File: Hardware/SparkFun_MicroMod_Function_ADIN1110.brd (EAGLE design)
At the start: 38 x 65 mm, 115 parts, among them J1 IP20(RJ50), J2 MICROMOD_FUNCTION_STANDARD, Q1 220mA/50V/3.5Ω, Q2 20V/4.2A/52mΩ/1.4W, T1 WE-STST, U1 ADIN1110, U2 EEPROM, U3 3.3V, U4 WE-TVS, Y1 25MHz

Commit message: R3, R4, R5, R6 to in-house PROD_IDs
Note, these values are very slightly different than the ones in the DS sch.
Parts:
- R3, R4: value 5.1Ω -> 4.7
- R5, R6: value 10.2Ω -> 10Ω
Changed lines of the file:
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@@
 <attribute name="VALUE" value="Blue" x="28.575040625" y="63.0764" size="0.6096" layer="27" font="vector" ratio="20" rot="R90" align="top-center"/>
 </element>
-<element name="R5" library="SparkFun-Resistors" package="0402-TIGHT" value="10.2Ω" x="20.812759375" y="39.8145" smashed="yes">
+<element name="R5" library="SparkFun-Resistors" package="0402-TIGHT" value="10Ω" x="20.812759375" y="39.8145" smashed="yes">
 <attribute name="NAME" x="20.812759375" y="40.3765" size="0.6096" layer="25" font="vector" ratio="20" align="bottom-center"/>
-<attribute name="VALUE" x="22.89301875" y="40.1542" size="0.6096" layer="27" font="vector" ratio="20" align="top-center"/>
+<attribute name="PROD_ID" value="RES-16072" x="20.812759375" y="39.8145" size="1.778" layer="27" display="off"/>
+<attribute name="VALUE" value="10Ω" x="22.89301875" y="40.1542" size="0.6096" layer="27" font="vector" ratio="20" align="top-center"/>
 </element>
-<element name="R6" library="SparkFun-Resistors" package="0402-TIGHT" value="10.2Ω" x="20.289521875" y="38.89501875" smashed="yes">
+<element name="R6" library="SparkFun-Resistors" package="0402-TIGHT" value="10Ω" x="20.289521875" y="38.89501875" smashed="yes">
 <attribute name="NAME" x="20.289521875" y="39.45701875" size="0.6096" layer="25" font="vector" ratio="20" align="bottom-center"/>
-<attribute name="VALUE" x="22.308821875" y="39.1661375" size="0.6096" layer="27" font="vector" ratio="20" align="top-center"/>
+<attribute name="PROD_ID" value="RES-16072" x="20.289521875" y="38.89501875" size="1.778" layer="27" display="off"/>
+<attribute name="VALUE" value="10Ω" x="22.308821875" y="39.1661375" size="0.6096" layer="27" font="vector" ratio="20" align="top-center"/>
 </element>
-<element name="R4" library="SparkFun-Resistors" package="0402-TIGHT" value="5.1Ω" x="22.501859375" y="42.4459375" smashed="yes" rot="R180">
+<element name="R4" library="SparkFun-Resistors" package="0402-TIGHT" value="4.7" x="22.501859375" y="42.4459375" smashed="yes" rot="R180">
 <attribute name="NAME" x="22.501859375" y="41.8839375" size="0.6096" layer="25" font="vector" ratio="20" rot="R180" align="bottom-center"/>
-<attribute name="VALUE" x="24.462740625" y="42.1697375" size="0.6096" layer="27" font="vector" ratio="20" rot="R180" align="top-center"/>
+<attribute name="PROD_ID" value="RES-16312" x="22.501859375" y="42.4459375" size="1.778" layer="27" rot="R180" display="off"/>
+<attribute name="VALUE" value="4.7" x="24.462740625" y="42.1697375" size="0.6096" layer="27" font="vector" ratio="20" rot="R180" align="top-center"/>
 </element>
-<element name="R3" library="SparkFun-Resistors" package="0402-TIGHT" value="5.1Ω" x="18.54961875" y="42.420540625" smashed="yes" rot="R180">
+<element name="R3" library="SparkFun-Resistors" package="0402-TIGHT" value="4.7" x="18.54961875" y="42.420540625" smashed="yes" rot="R180">
 <attribute name="NAME" x="18.54961875" y="41.858540625" size="0.6096" layer="25" font="vector" ratio="20" rot="R180" align="bottom-center"/>
-<attribute name="VALUE" x="16.624296875" y="42.1672" size="0.6096" layer="27" font="vector" ratio="20" rot="R180" align="top-center"/>
+<attribute name="PROD_ID" value="RES-16312" x="18.54961875" y="42.420540625" size="1.778" layer="27" rot="R180" display="off"/>
+<attribute name="VALUE" value="4.7" x="16.624296875" y="42.1672" size="0.6096" layer="27" font="vector" ratio="20" rot="R180" align="top-center"/>
 </element>
 <element name="C2" library="SparkFun-Capacitors" package="0603" value="0.22uF" x="18.7934625" y="43.6981625" smashed="yes">

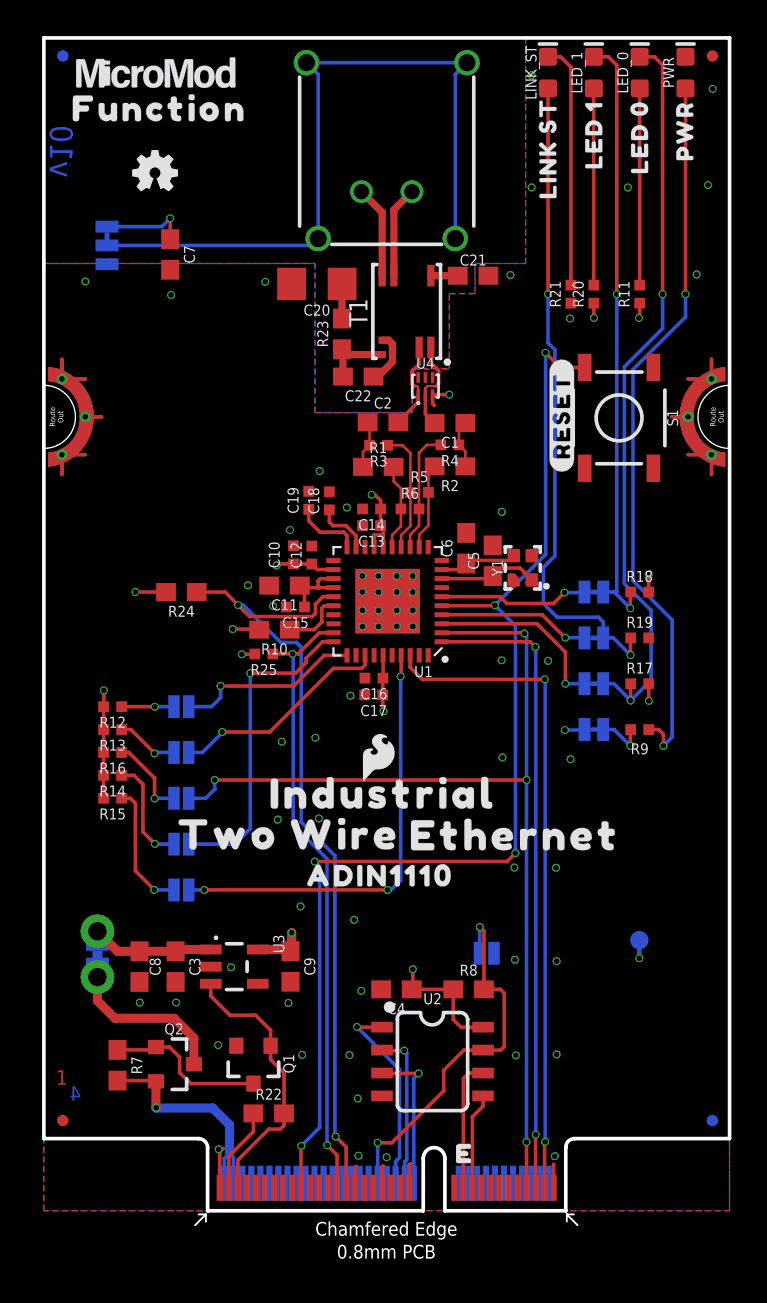
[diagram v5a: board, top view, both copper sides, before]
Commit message: TVS diode placement and more
-Moved TVS diodes to "IC" side of DA-/DA+ DC coupling caps
-Added debounce to reset button
-Routed through pads 5 and 6 on TVS diode package.
-Added R29 to avoid damaging GPIO if set to output low and button pressed
-Added R26 to mosfet gate control line to avoid potential overvoltage/ringing
-Re-arranged caps so smalled value decoupling caps are closest to pins on IC.
-moved to "v10" in brd and sch
-C22 changed to 470nF to improove droop performance
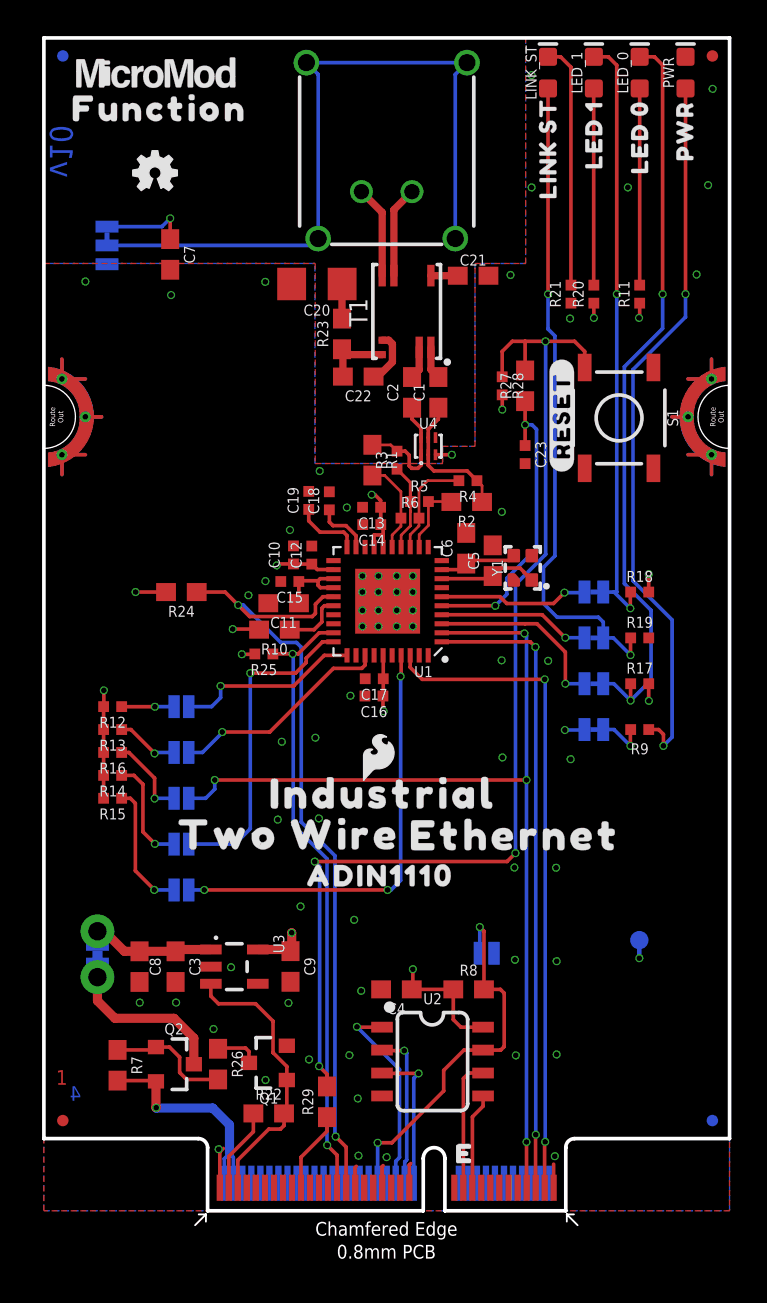
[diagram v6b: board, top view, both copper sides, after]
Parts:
- added C23: 0.1uF, SparkFun-Capacitors:0402-TIGHT
- added R26: 100, SparkFun-Resistors:0603
- added R27: 10k, SparkFun-Resistors:0603
- added R28: 100k, SparkFun-Resistors:0402-TIGHT
- added R29: 100Ω, SparkFun-Resistors:0603
- C22: value 0.1uF -> 470nF
- R3, R4: value 4.7 -> 5.1k
- R5, R6: value 10Ω -> 10.2k
- moved U4 3.33 mm to (21.3, 42.4)
- moved C2 2.31 mm to (20.4, 45.4), turned to 90 degrees
- moved R4 2.22 mm to (23.5, 40.5)
- moved R2 2.18 mm to (23.4, 39.3)
- moved C1 1.82 mm to (21.9, 45.4), turned to 90 degrees
- moved C15 1.44 mm to (13.6, 34.9)
- moved R3 1.31 mm to (19.6, 41.6), turned to 90 degrees
- moved C13 1.01 mm to (18.2, 39.0)
- moved C16 0.99 mm to (18.3, 28.5)
- moved C11 0.98 mm to (13.3, 33.7)
- moved C17 0.90 mm to (18.3, 29.5)
- moved C14 0.87 mm to (18.2, 38.0)
- moved Q1 0.85 mm to (12.5, 8.20), turned to 90 degrees
- moved R5 0.51 mm to (20.8, 39.3)
- moved R6 0.51 mm to (20.3, 38.4)
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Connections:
- new net N$10: Q1.3, R26.1
- new net N$13: C23.1, R27.1, U1.5
- new net N$15: R27.2, R28.1, R29.2, S1.3
- net !RESET!: now also R29.1; no longer S1.3, U1.5
- net 3.3V: now also R28.2
- net GND: now also C23.2
- net N$11: now also R26.2; no longer Q1.3
- net N$24: now also U4.2, U4.5
- net N$31: now also U4.1, U4.6
- net N$32: no longer U4.2
- net N$34: no longer U4.1
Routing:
- net N$15: track 0.00 -> 62.1 mm, vias 0 -> 4
- net !RESET!: track 64.8 -> 4.51 mm, vias 5 -> 0
- net N$13: track 0.00 -> 16.9 mm, vias 0 -> 2
- net N$24: track 2.69 -> 7.77 mm
- net N$31: track 2.67 -> 7.05 mm
- net N$32: track 5.18 -> 1.81 mm
- net N$34: track 4.99 -> 1.80 mm
- net N$10: track 0.00 -> 2.44 mm
- net N$11: track 8.93 -> 6.87 mm
- net N$36: track 6.86 -> 4.83 mm
- net N$35: track 6.82 -> 5.82 mm
- net 3.3V: track 36.4 -> 37.3 mm, vias 15 -> 16
- net N$38: track 4.83 -> 4.02 mm
- net GND: track 9.56 -> 9.04 mm, vias 64 -> 65
- net PWR_EN: track 15.3 -> 15.8 mm

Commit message: 470pF cap to 0805 with new PROD_ID
-new 470nF cap had to bump up to 0805 for the 100V rating in that value
-Voltage specs in part values
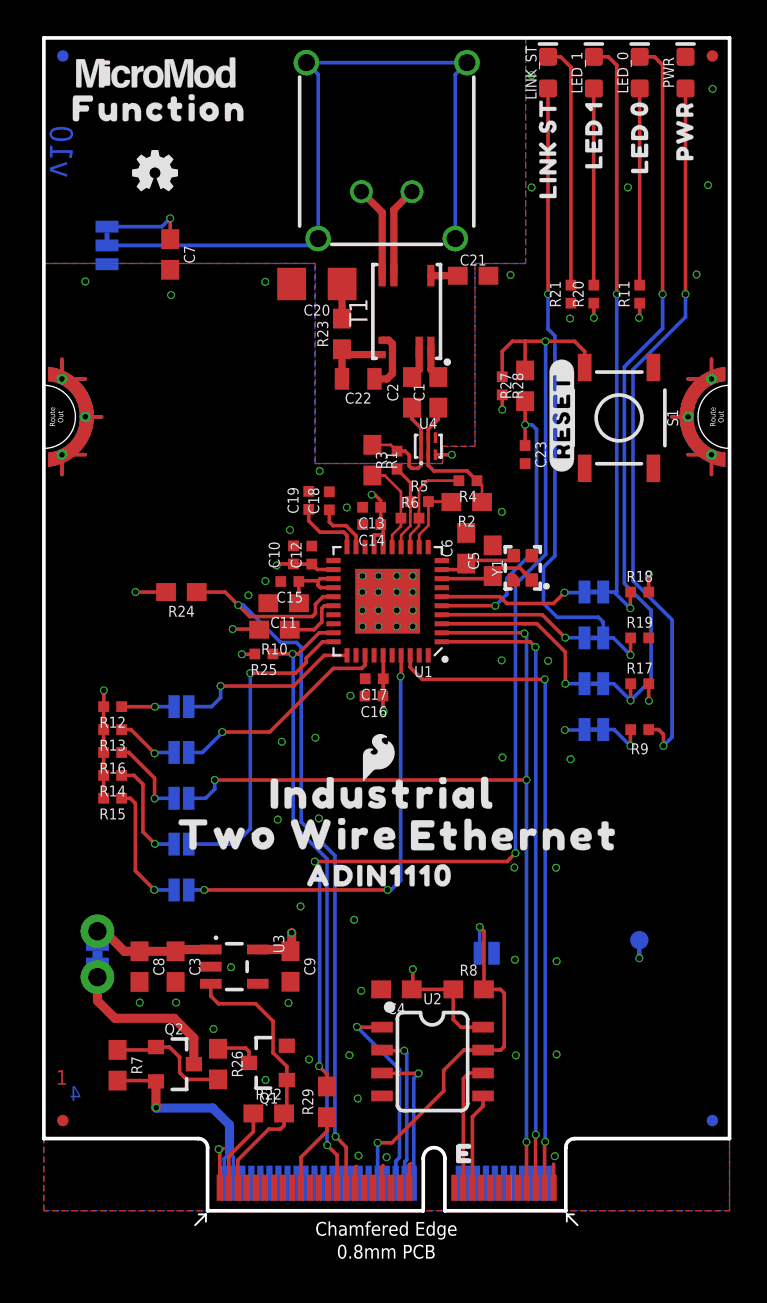
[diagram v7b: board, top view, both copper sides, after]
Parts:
- C21: value 0.1uF -> 0.1uF/50V
- C22: value 470nF -> 470nF/100V; device SparkFun-Capacitors:0603 -> SparkFun-Capacitors:0805
- moved C22 0.13 mm to (17.4, 46.1)

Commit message: SPI test points and moved config jumpers
-moved bottom config jumpers to avoid reflections on CIPO
-added SPI test points
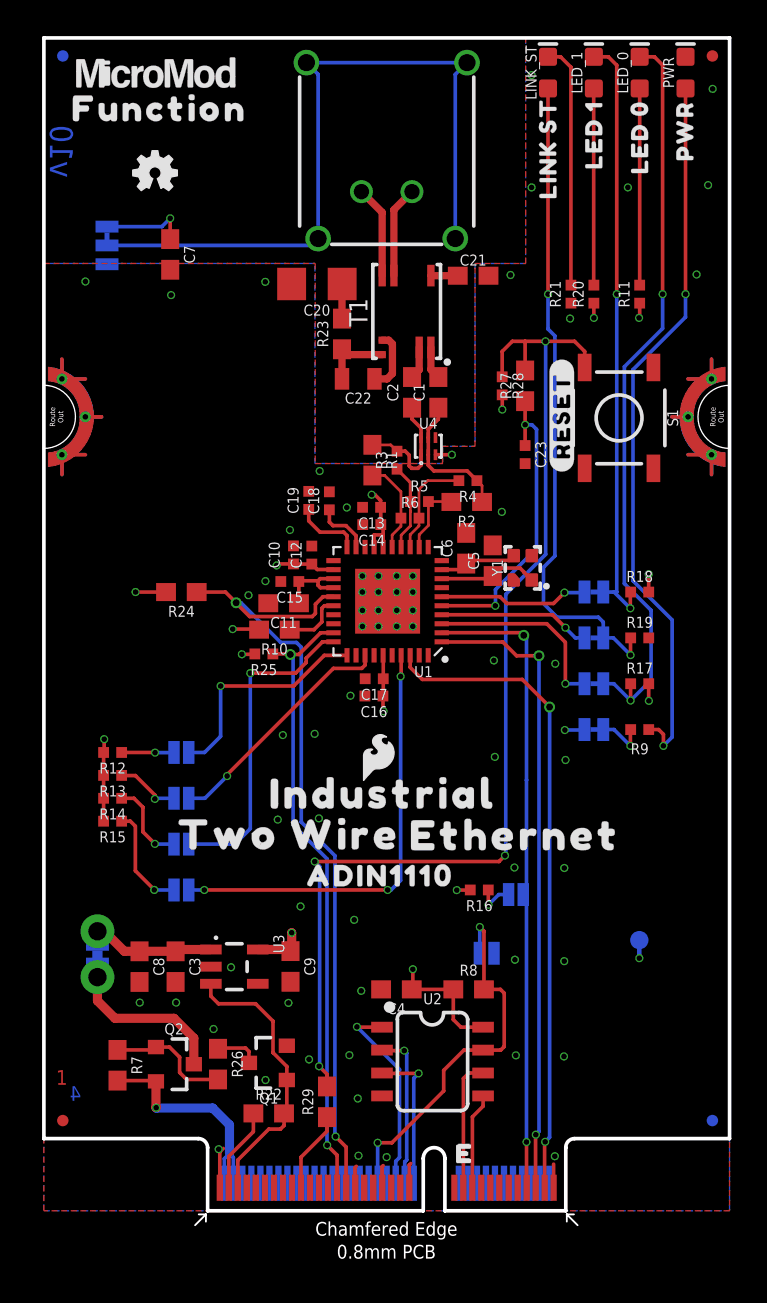
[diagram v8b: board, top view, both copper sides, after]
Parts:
- added CIPO, COPI, CS, INT, SPI: (no value), SparkFun-Connectors:TP_15TH
- moved R16 21.7 mm to (24.1, 17.8)
- moved SPI_CFG0 19.3 mm to (26.2, 17.5)
- moved U$16 19.3 mm to (30.9, 17.5)
- moved R12 2.54 mm to (3.81, 25.4)
- moved R13 2.54 mm to (3.81, 24.1)
- moved TX2P4 2.54 mm to (7.62, 25.4)
- moved SWPD 2.54 mm to (7.62, 22.9)
- moved U$13 2.54 mm to (12.7, 25.4)
- moved U$22 2.54 mm to (12.4, 22.9)
- moved R14 1.27 mm to (3.81, 22.9)
- moved R15 1.27 mm to (3.81, 21.6)
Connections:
- net !CS!: now also CS.1
- net !INT!: now also INT.1
- net SPI_CIPO/SPI_CFG0: now also CIPO.1
- net SPI_COPI: now also COPI.1
- net SPI_SCK: now also SPI.1
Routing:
- net SPI_CIPO/SPI_CFG0: track 54.8 -> 35.5 mm, vias 4 -> 1
- net N$28: track 4.62 -> 2.18 mm
- net !TX2P4_EN!: track 10.3 -> 12.6 mm
- net N$29: track 7.21 -> 5.94 mm
- net N$25: track 6.03 -> 4.76 mm
- net !SWPD_EN!: track 12.3 -> 13.4 mm
- net 3.3V: track 37.3 -> 36.6 mm, vias 16 -> 17
- net SPI_SCK: track 36.6 -> 36.1 mm, vias 2 -> 1
- net !INT!: track 44.3 -> 44.5 mm, vias 2 -> 1
- net !CS!: vias 2 -> 1
- net SPI_COPI: vias 2 -> 1
